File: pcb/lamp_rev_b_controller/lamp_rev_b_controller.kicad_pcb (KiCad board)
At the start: 4 copper layers, 118 x 94 mm, 155 parts, among them J1 TYPE-C 3.1 MT 16P, J10 2-pin NTC header, J11 2-pin NTC header, J12 DB128H-5.08-2P-BK-S, J13 DB128H-5.08-2P-BK-S, J15 DB128H-5.08-2P-BK-S, J16 LED NTC/ID header, J17 External camera sync header, J18 SPI/FIFO camera module header, J19 Lid/cartridge/cutoff interloc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, J2 DB128H-5.08-2P-BK-S, J20 Fan PWM/tach header, J21 2x3 UART/programming header, J22 I2C expansion header, J23 Analog optical diagnostic hea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, J24 DB128H-5.08-2P high-current h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, J4 2-pin NTC header, J5 2-pin NTC header, J6 2-pin NTC header, J7 2-pin NTC header, J8 2-pin NTC header, J9 2-pin NTC header, Q1 IRLB3813PBF TO-220 12V protot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, Q2 IRLB3813PBF TO-220 12V protot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, U1 ESP32-S3-WROOM-1-N16, U10 INA180A1IDBVR gain 20 LED cur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, U2 USBLC6-2SC6, U3 Diodes AP63203WU-7 fixed 3.3V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, U4 ADS1115IDGSR, U5 CD74HC4051M, U6 TC4427ACOA/TC4427EPA, U7 CUI/Bel P7805-2000-S 5V 2A 8-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, U8 Mean Well LDD-700H 700mA CC b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, U9 SN74LVC1G08DBVR LED_EXC_PWM A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

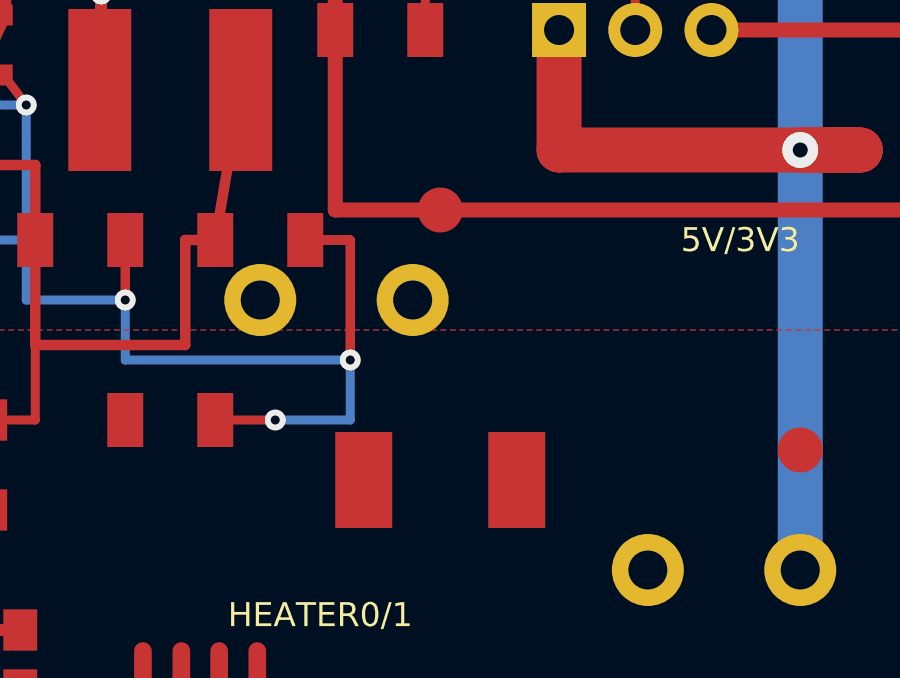
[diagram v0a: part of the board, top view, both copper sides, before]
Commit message: Close Rev B LED_PLUS route open
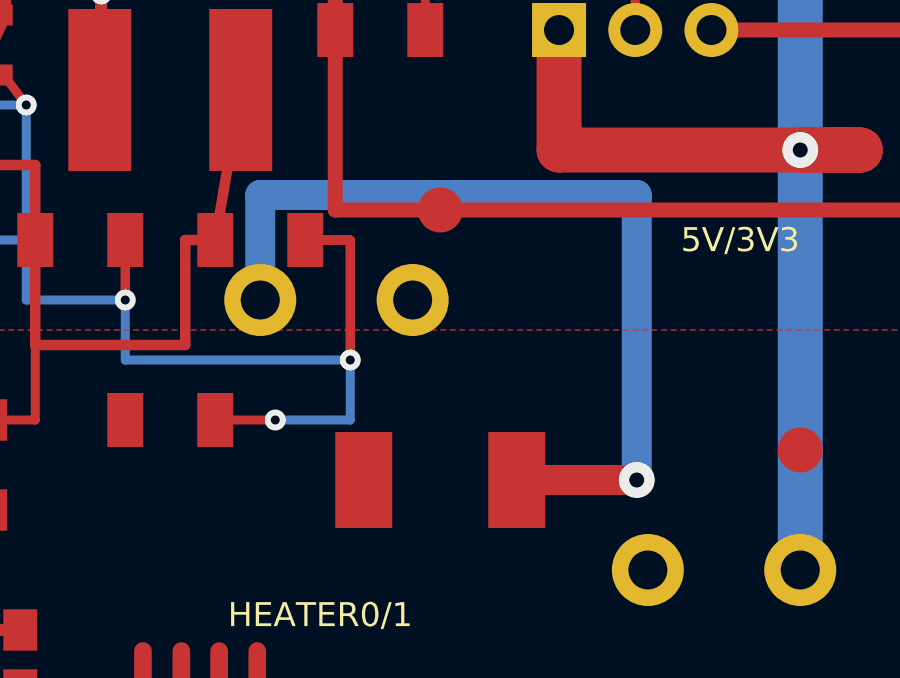
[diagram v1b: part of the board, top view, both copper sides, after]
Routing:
- net LED_PLUS: track 0.00 -> 29.5 mm, vias 0 -> 1
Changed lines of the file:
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@@
+  )
+  (via
+    (at 106.550 39)
+    (size 1.200)
+    (drill 0.500)
+    (layers "F.Cu" "B.Cu")
+    (net 57)
   )
   (via
@@
   )
   (segment
+    (start 102.550 39)
+    (end 106.550 39)
+    (width 1)
+    (layer "F.Cu")
+    (net 57)
+  )
+  (segment
+    (start 106.550 39)
+    (end 106.550 29.500)
+    (width 1)
+    (layer "B.Cu")
+    (net 57)
+  )
+  (segment
+    (start 106.550 29.500)
+    (end 94 29.500)
+    (width 1)
+    (layer "B.Cu")
+    (net 57)
+  )
+  (segment
+    (start 94 29.500)
+    (end 94 33)
+    (width 1)
+    (layer "B.Cu")
+    (net 57)
+  )
+  (segment

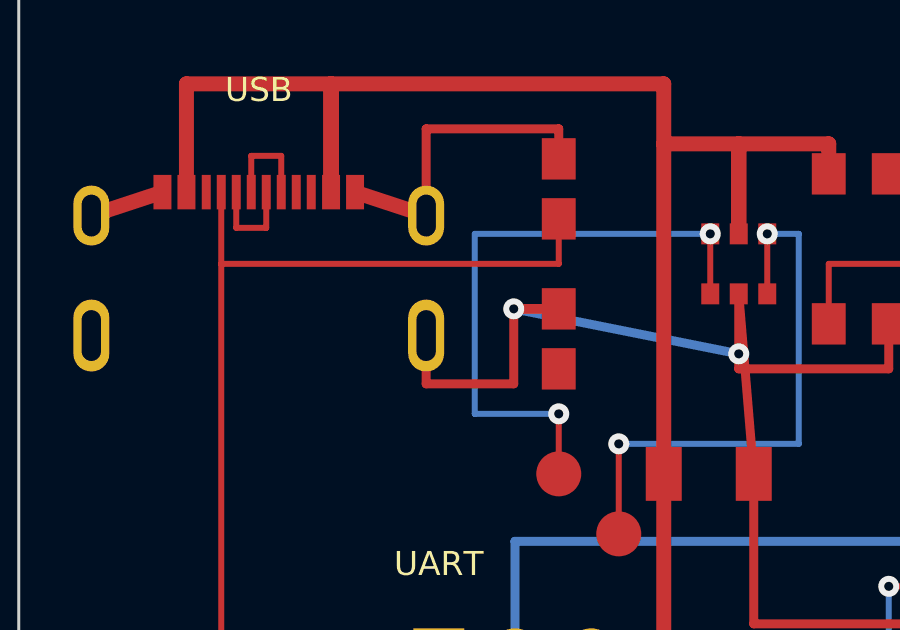
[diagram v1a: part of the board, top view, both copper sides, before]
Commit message: Close Rev B USB_CC2 route open
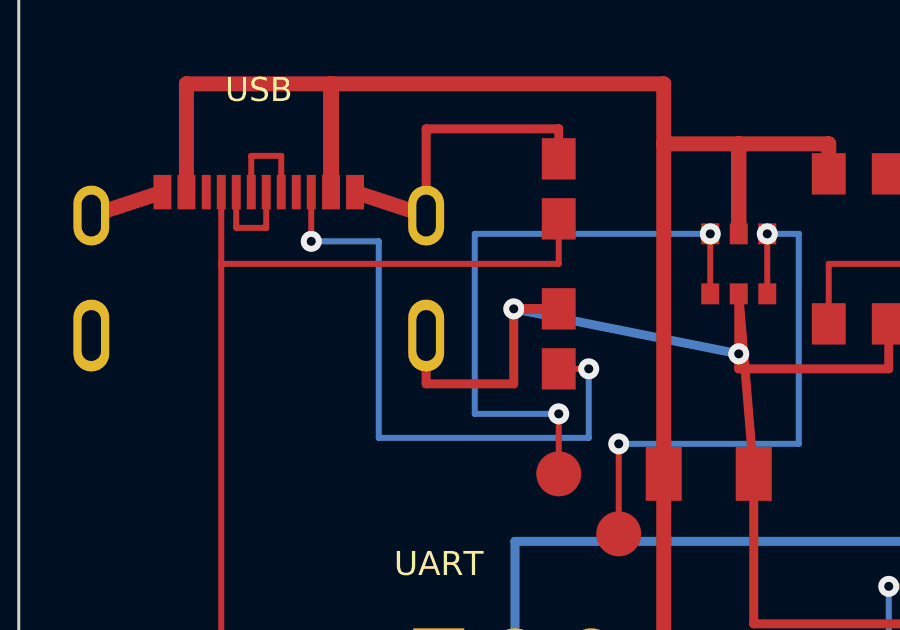
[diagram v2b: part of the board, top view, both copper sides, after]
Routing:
- net USB_CC2: track 0.00 -> 20.7 mm, vias 0 -> 2
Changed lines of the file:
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@@
+  )
+  (via
+    (at 9.750 7.250)
+    (size 0.700)
+    (drill 0.300)
+    (layers "F.Cu" "B.Cu")
+    (net 16)
+  )
+  (via
+    (at 19 11.500)
+    (size 0.700)
+    (drill 0.300)
+    (layers "F.Cu" "B.Cu")
+    (net 16)
   )
   (via
@@
   )
   (segment
+    (start 9.750 5.610)
+    (end 9.750 7.250)
+    (width 0.200)
+    (layer "F.Cu")
+    (net 16)
+  )
+  (segment
+    (start 9.750 7.250)
+    (end 12 7.250)
+    (width 0.200)
+    (layer "B.Cu")
+    (net 16)
+  )
+  (segment
+    (start 12 7.250)
+    (end 12 13.800)
+    (width 0.200)
+    (layer "B.Cu")
+    (net 16)
+  )
+  (segment
+    (start 12 13.800)
+    (end 19 13.800)
+    (width 0.200)
+    (layer "B.Cu")
+    (net 16)
+  )
+  (segment
+    (start 19 13.800)
+    (end 19 11.500)
+    (width 0.200)
+    (layer "B.Cu")
+    (net 16)
+  )
+  (segment
+    (start 19 11.500)
+    (end 18 11.500)
+    (width 0.200)
+    (layer "F.Cu")
+    (net 16)
+  )
+  (segment

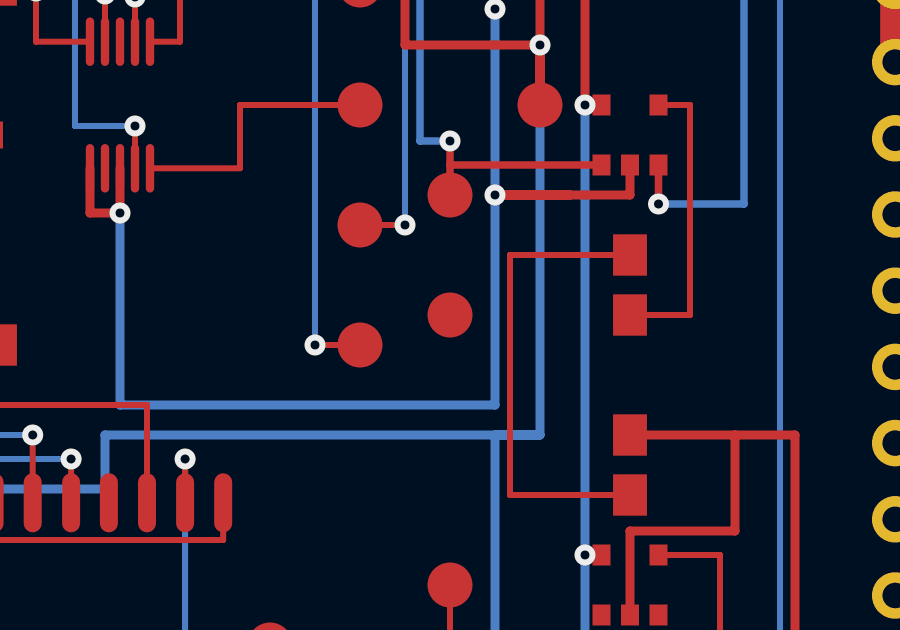
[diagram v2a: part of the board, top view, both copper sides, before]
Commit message: Close LED_EXC_EN Rev B controller route
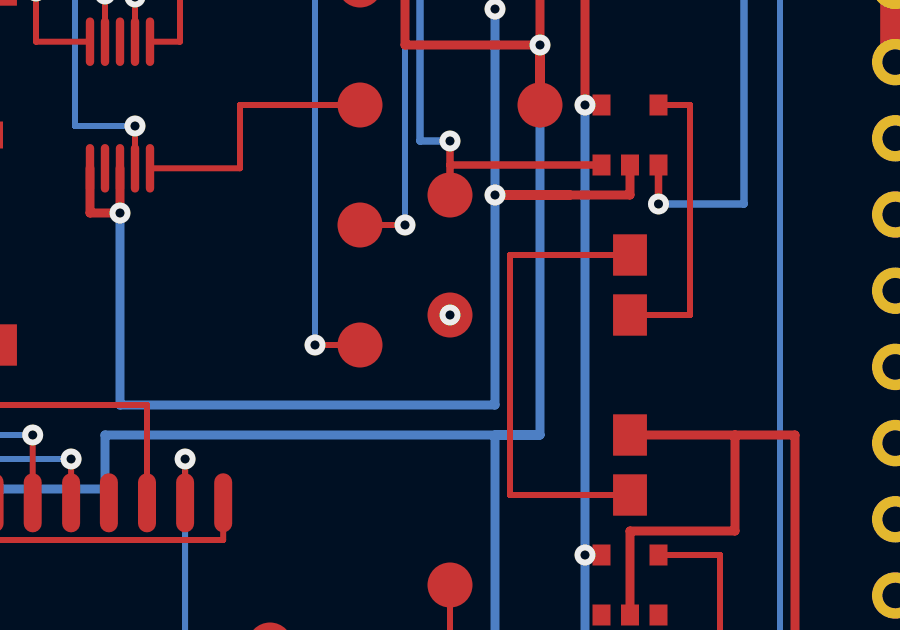
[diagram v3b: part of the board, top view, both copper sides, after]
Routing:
- net LED_EXC_EN: track 37.1 -> 45.0 mm, vias 2 -> 3
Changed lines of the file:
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@@
   )
   (via
+    (at 41 49)
+    (size 0.700)
+    (drill 0.300)
+    (layers "F.Cu" "B.Cu")
+    (net 50)
+  )
+  (via
     (at 29.630 62)
     (size 0.700)
@@
     (net 50)
   )
+  (segment
+    (start 41 49)
+    (end 47.950 45.300)
+    (width 0.250)
+    (layer "In2.Cu")
+    (net 50)
+  )

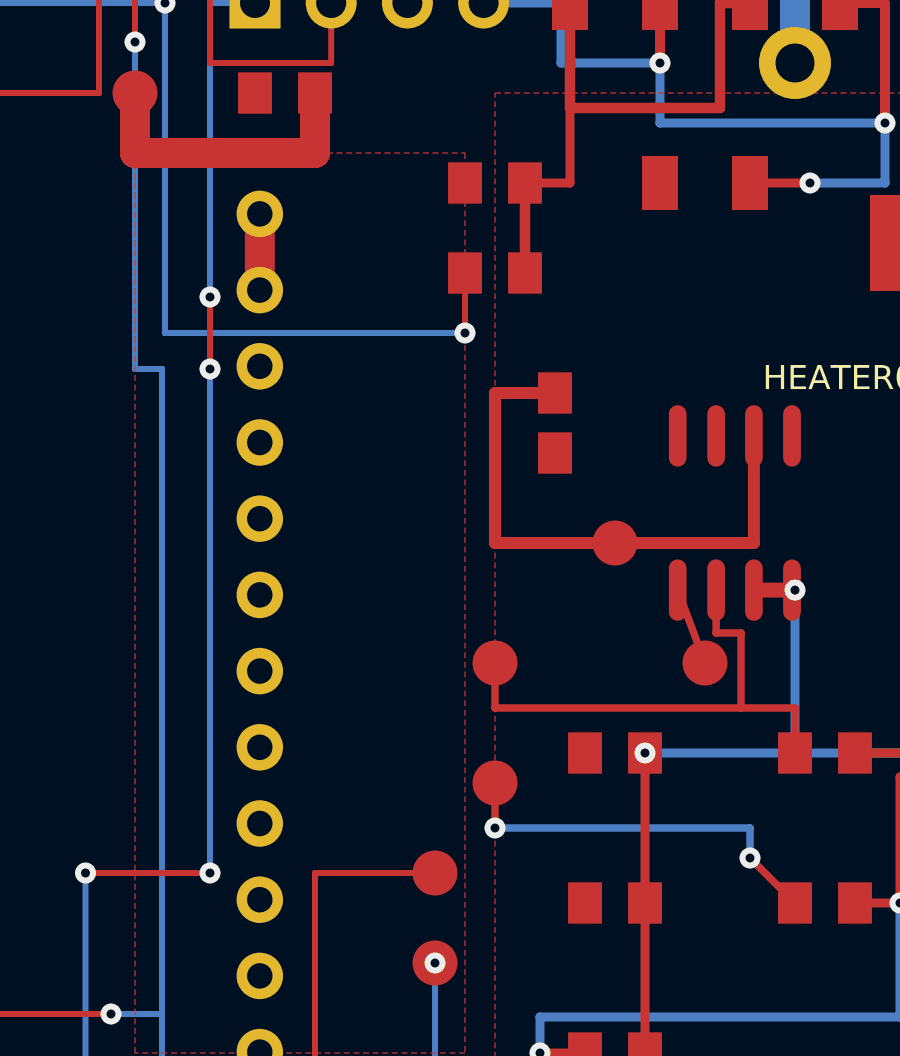
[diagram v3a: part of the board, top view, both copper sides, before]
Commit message: Close CAM_CS_N route on Rev B controller
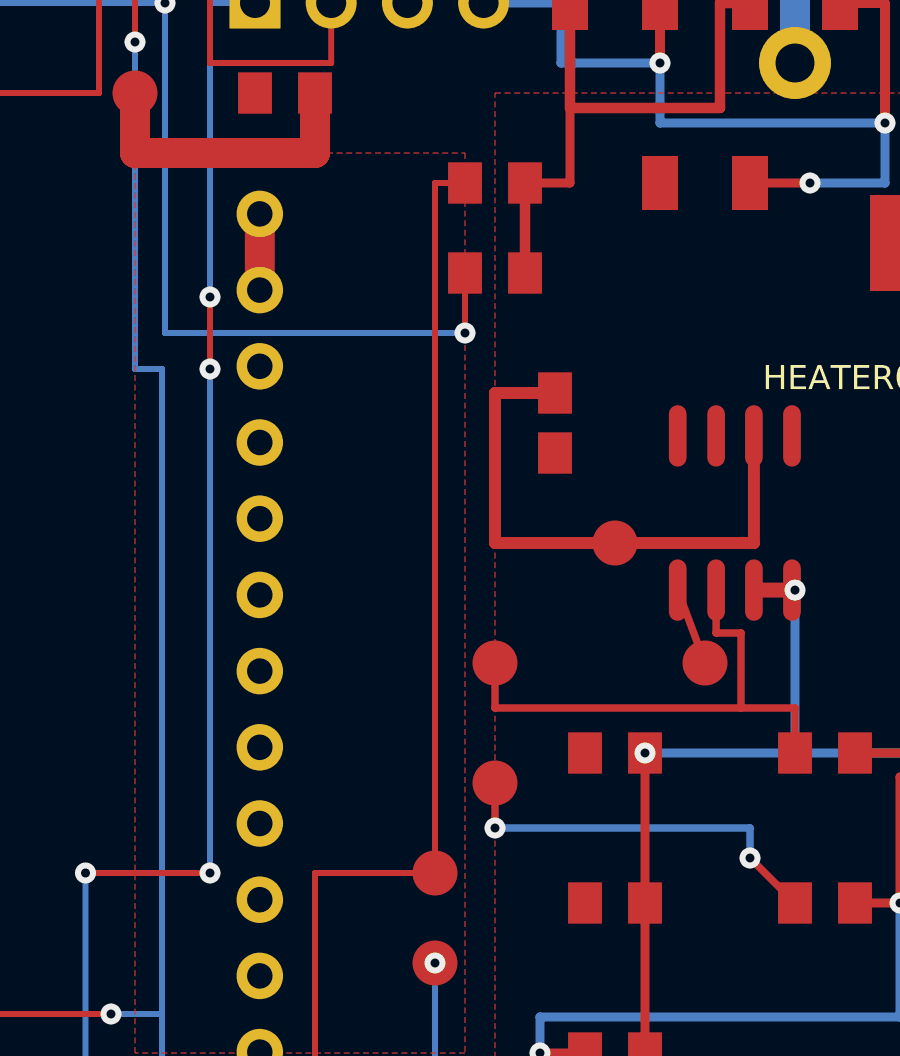
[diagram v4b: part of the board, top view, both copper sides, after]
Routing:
- net CAM_CS_N: track 24.3 -> 48.3 mm
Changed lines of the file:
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@@
+  )
+  (segment
+    (start 82 60)
+    (end 82 37)
+    (width 0.200)
+    (layer "F.Cu")
+    (net 27)
+  )
+  (segment
+    (start 82 37)
+    (end 83 37)
+    (width 0.200)
+    (layer "F.Cu")
+    (net 27)
   )
   (segment

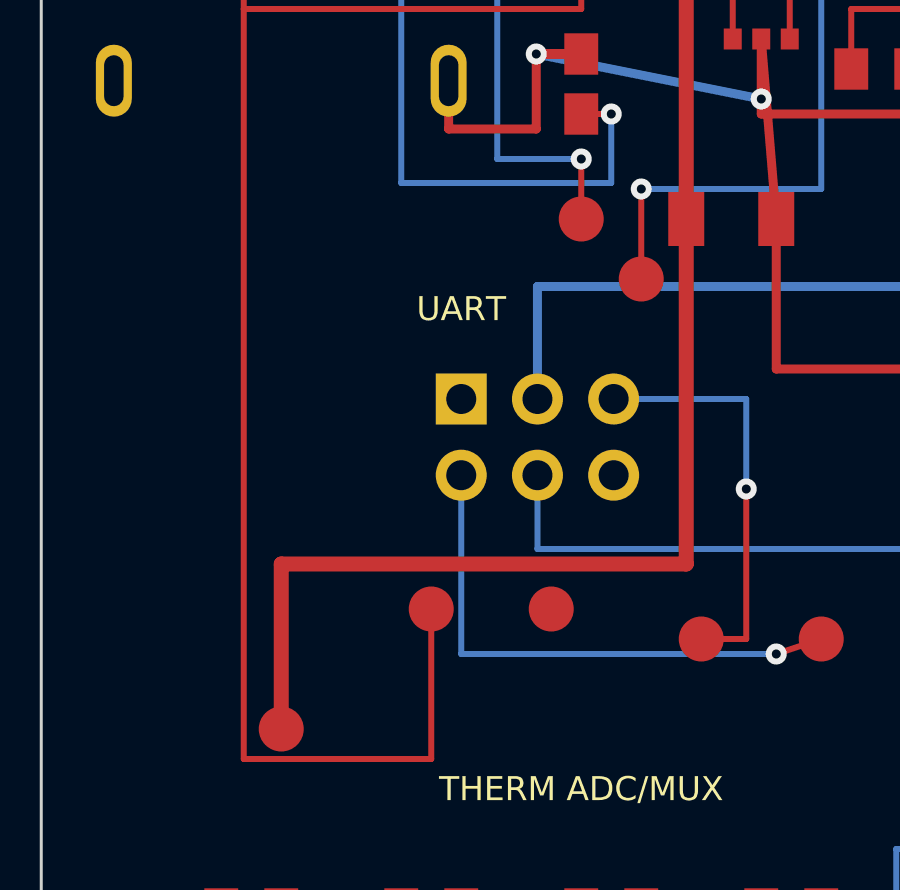
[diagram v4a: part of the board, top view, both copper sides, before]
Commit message: Close Rev B USB_CC2 TP branch route
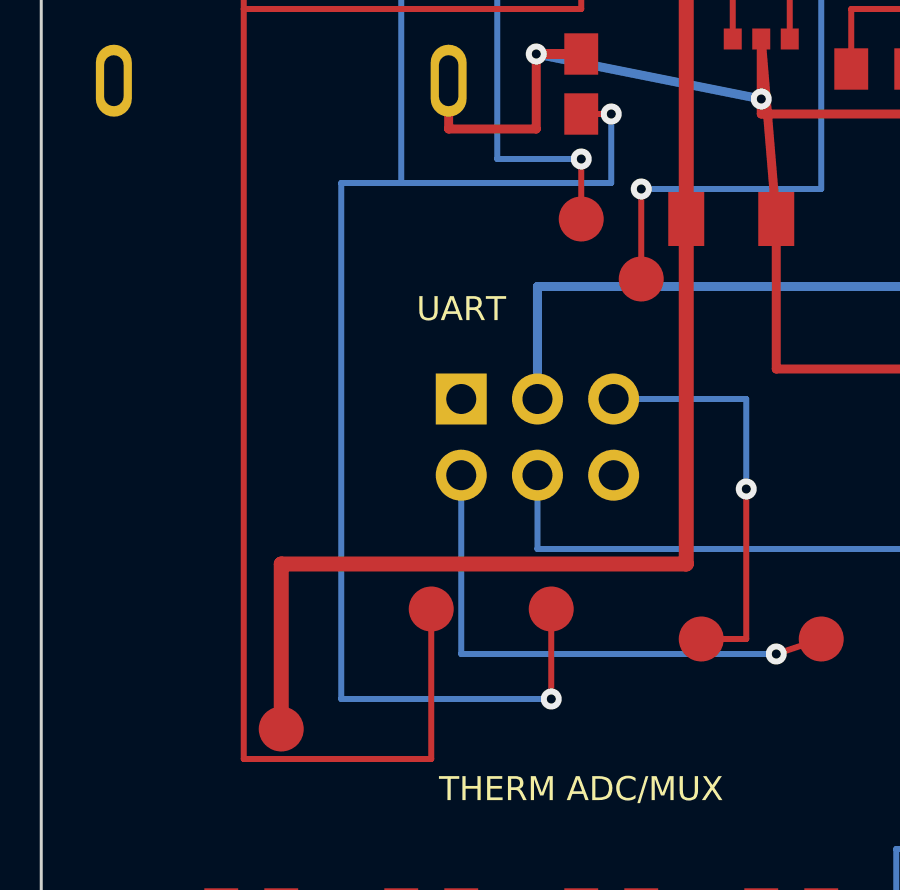
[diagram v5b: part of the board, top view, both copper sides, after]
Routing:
- net USB_CC2: track 20.7 -> 49.9 mm, vias 2 -> 3
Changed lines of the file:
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@@
+  )
+  (via
+    (at 17 31)
+    (size 0.700)
+    (drill 0.300)
+    (layers "F.Cu" "B.Cu")
+    (net 16)
   )
   (via
@@
     (net 16)
   )
+  (segment
+    (start 17 28)
+    (end 17 31)
+    (width 0.200)
+    (layer "F.Cu")
+    (net 16)
+  )
+  (segment
+    (start 17 31)
+    (end 10 31)
+    (width 0.200)
+    (layer "B.Cu")
+    (net 16)
+  )
+  (segment
+    (start 10 31)
+    (end 10 13.800)
+    (width 0.200)
+    (layer "B.Cu")
+    (net 16)
+  )
+  (segment
+    (start 10 13.800)
+    (end 12 13.800)
+    (width 0.200)
+    (layer "B.Cu")
+    (net 16)
+  )

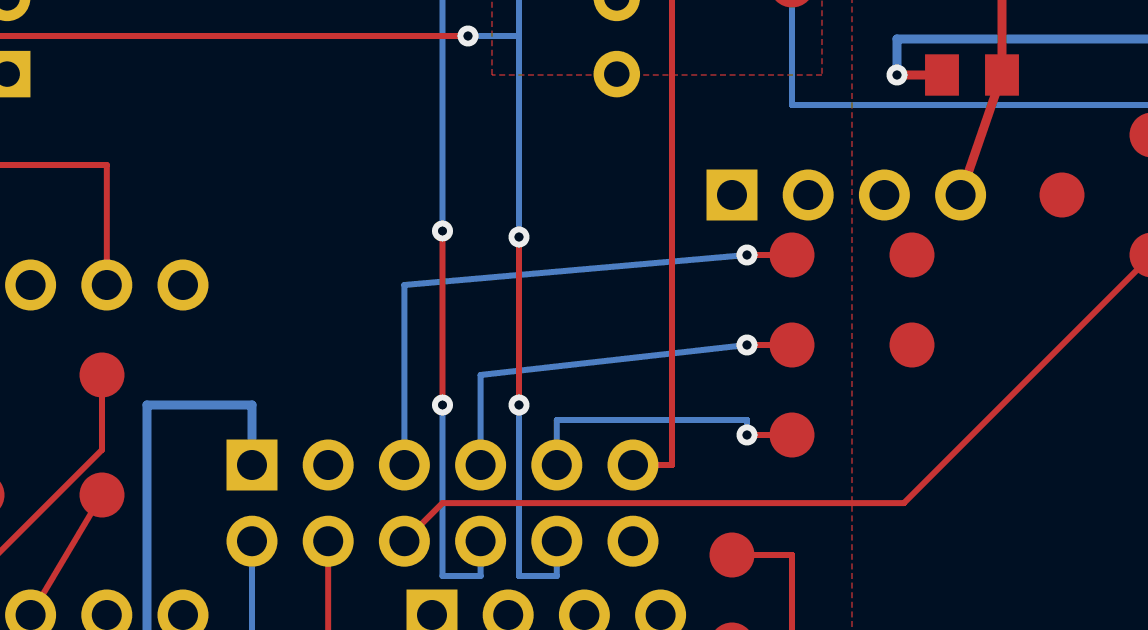
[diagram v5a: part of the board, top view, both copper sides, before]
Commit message: Close Rev B SPARE_GPIO42 TP branch
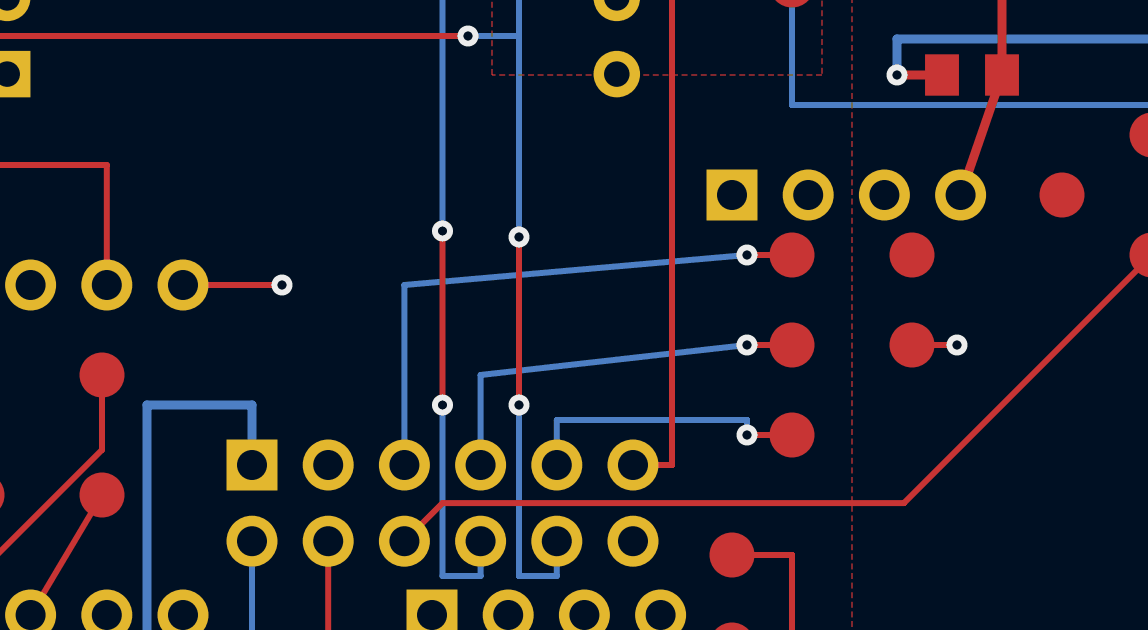
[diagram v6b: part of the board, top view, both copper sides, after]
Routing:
- net SPARE_GPIO42: track 0.00 -> 29.3 mm, vias 0 -> 2
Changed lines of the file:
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@@
     (net 22)
   )
+  (via
+    (at 65 73)
+    (size 0.700)
+    (drill 0.300)
+    (layers "F.Cu" "B.Cu")
+    (net 70)
+  )
+  (via
+    (at 87.500 75)
+    (size 0.700)
+    (drill 0.300)
+    (layers "F.Cu" "B.Cu")
+    (net 70)
+  )
   (segment
     (start 32.170 60.740)
@@
     (net 74)
   )
+  (segment
+    (start 61.700 73)
+    (end 65 73)
+    (width 0.200)
+    (layer "F.Cu")
+    (net 70)
+  )
+  (segment
+    (start 65 73)
+    (end 78 73)
+    (width 0.200)
+    (layer "In2.Cu")
+    (net 70)
+  )
+  (segment
+    (start 78 73)
+    (end 78 74.200)
+    (width 0.200)
+    (layer "In2.Cu")
+    (net 70)
+  )
+  (segment
+    (start 78 74.200)
+    (end 87.500 74.200)
+    (width 0.200)
+    (layer "In2.Cu")
+    (net 70)
+  )
+  (segment
+    (start 87.500 74.200)
+    (end 87.500 75)
+    (width 0.200)
+    (layer "In2.Cu")
+    (net 70)
+  )
+  (segment
+    (start 87.500 75)
+    (end 86 75)
+    (width 0.200)
+    (layer "F.Cu")
+    (net 70)
+  )
   (zone
